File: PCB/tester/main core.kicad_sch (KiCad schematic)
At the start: 44 parts, among them J2 PR20203VBDN, Q1 DMN63D8L-7, SW1 TL3305BF260QG, SW2 TL3305BF260QG, SW3 TL3305BF260QG, SW4 TL3305BF260QG, SW5 TL3305BF260QG, SW6 TL3305BF260QG, SW7 TL3305BF260QG, SW8 TL3305BF260QG, SW9 TL3305BF260QG, U5 ATXMEGA32A4U-MH

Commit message: Update 1N4148 part numbers
Replace obsolete 1N4148 :
OEPS030017 -> OEPS030052
1N4148WX-TP -> 1N4148WS-E3-18
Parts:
- D5: MPN 1N4148WX-TP -> 1N4148WS-E3-18; OEPSPN OEPS030017 -> OEPS030052
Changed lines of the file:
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@@
 			)
 		)
-		(property "OEPSPN" "OEPS030017"
+		(property "OEPSPN" "OEPS030052"
 			(at 254 143.51 90)
 			(hide yes)
@@
 			)
 		)
-		(property "MPN" "1N4148WX-TP"
+		(property "MPN" "1N4148WS-E3-18"
 			(at 254 143.51 90)
 			(hide yes)

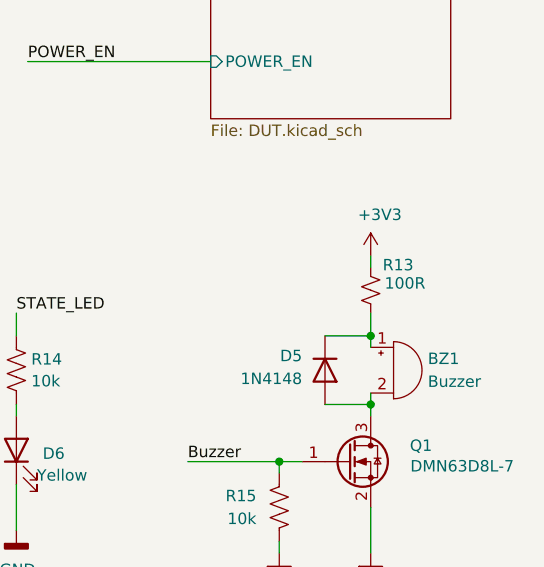
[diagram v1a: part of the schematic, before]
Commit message: Replace R13 100R with 1R and update BOM/metadata
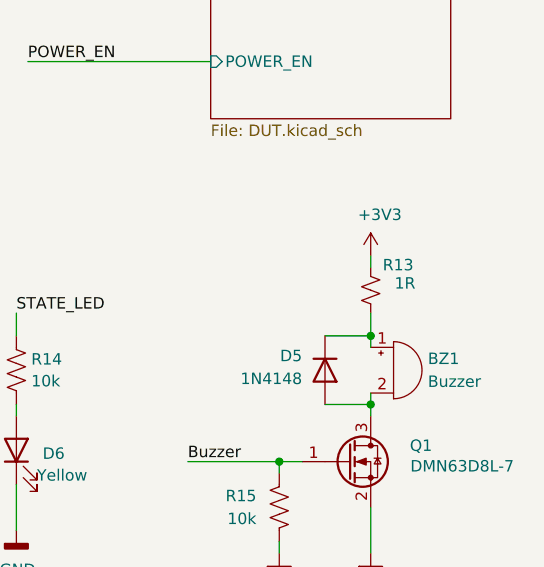
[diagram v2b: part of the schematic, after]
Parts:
- R13: value 100R -> 1R; MPN RCS0402100RFKED -> CRCW04021R00FKEDHP; OEPSPN OEPS020028 -> OEPS020224
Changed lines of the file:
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@@
 			)
 		)
-		(property "Value" "100R"
+		(property "Value" "1R"
 			(at 262.89 133.858 0)
 			(show_name no)
@@
 			)
 		)
-		(property "Description" "RESISTOR:   SMD 0402 100Ω ±1% 0.250W   [RCS0402100RFKED] [SMD]"
+		(property "Description" "RESISTOR:   SMD 0402 1Ω ±1% 0.200W   [CRCW04021R00FKEDHP] [SMD]"
 			(at 259.08 134.62 0)
 			(hide yes)
@@
 			)
 		)
-		(property "MPN" "RCS0402100RFKED"
+		(property "MPN" "CRCW04021R00FKEDHP"
 			(at 259.08 134.62 90)
 			(hide yes)
@@
 			)
 		)
-		(property "OEPSPN" "OEPS020028"
+		(property "OEPSPN" "OEPS020224"
 			(at 259.08 134.62 90)
 			(hide yes)
